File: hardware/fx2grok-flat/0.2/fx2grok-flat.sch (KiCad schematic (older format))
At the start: 32 parts, among them IC1 CY7C68013A-56, J1 Conn_02x05_Odd_Even, P1 pkl_USB_OTG, U1 3.3V, U2 USBLC6-2, U3 DSILC6-4, U4 DSILC6-4, X1 24MHz

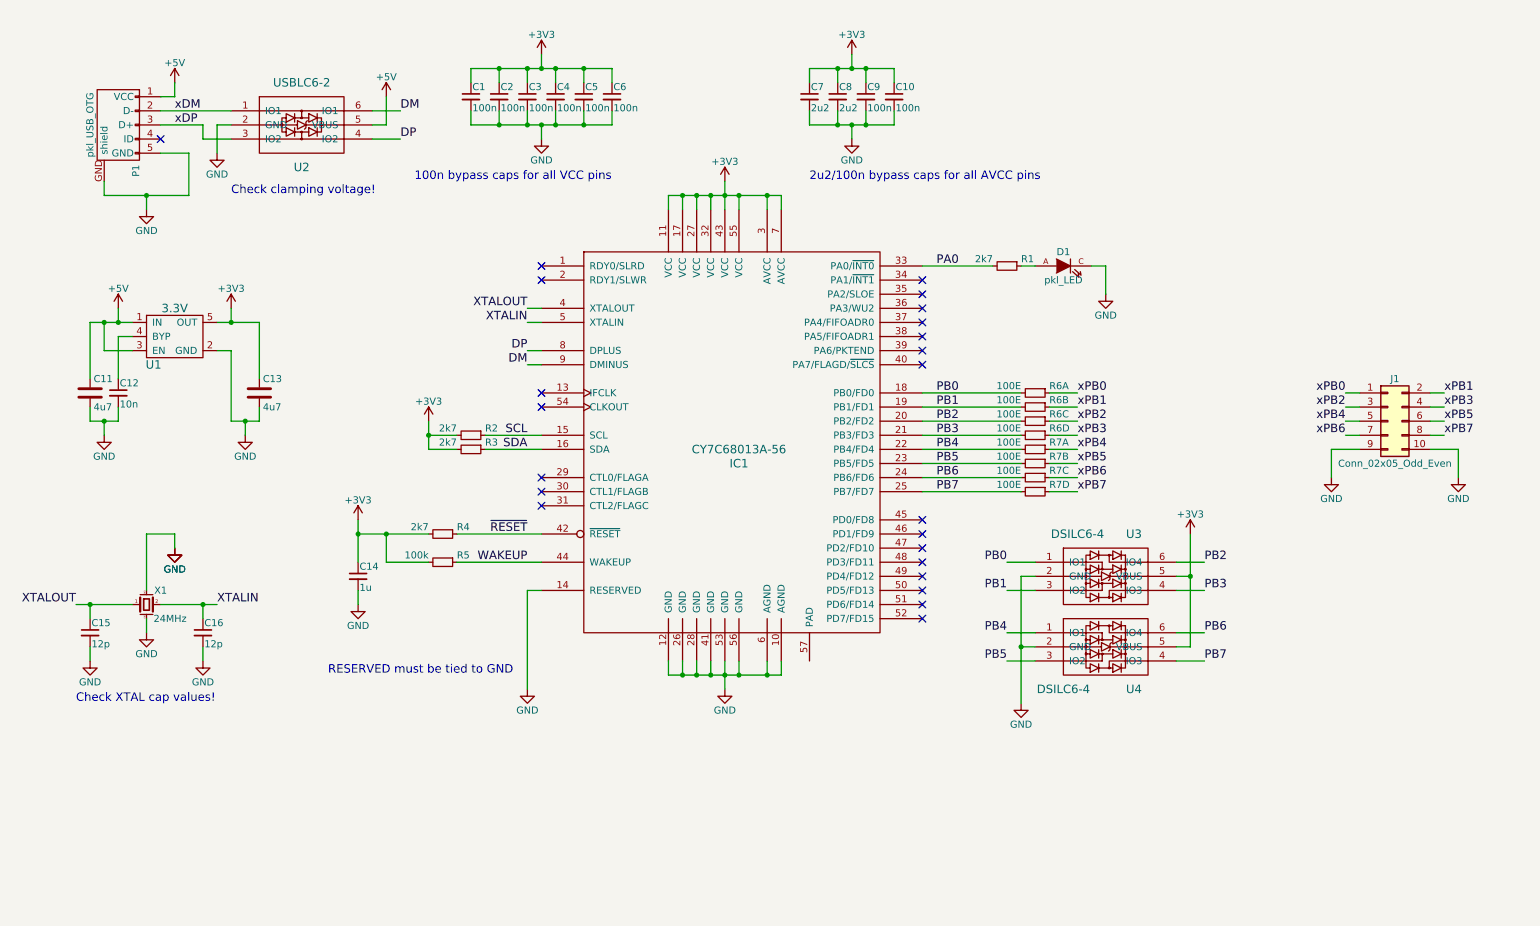
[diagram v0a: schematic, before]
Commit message: Added eeprom and pullups on probe inputs. Started routing.
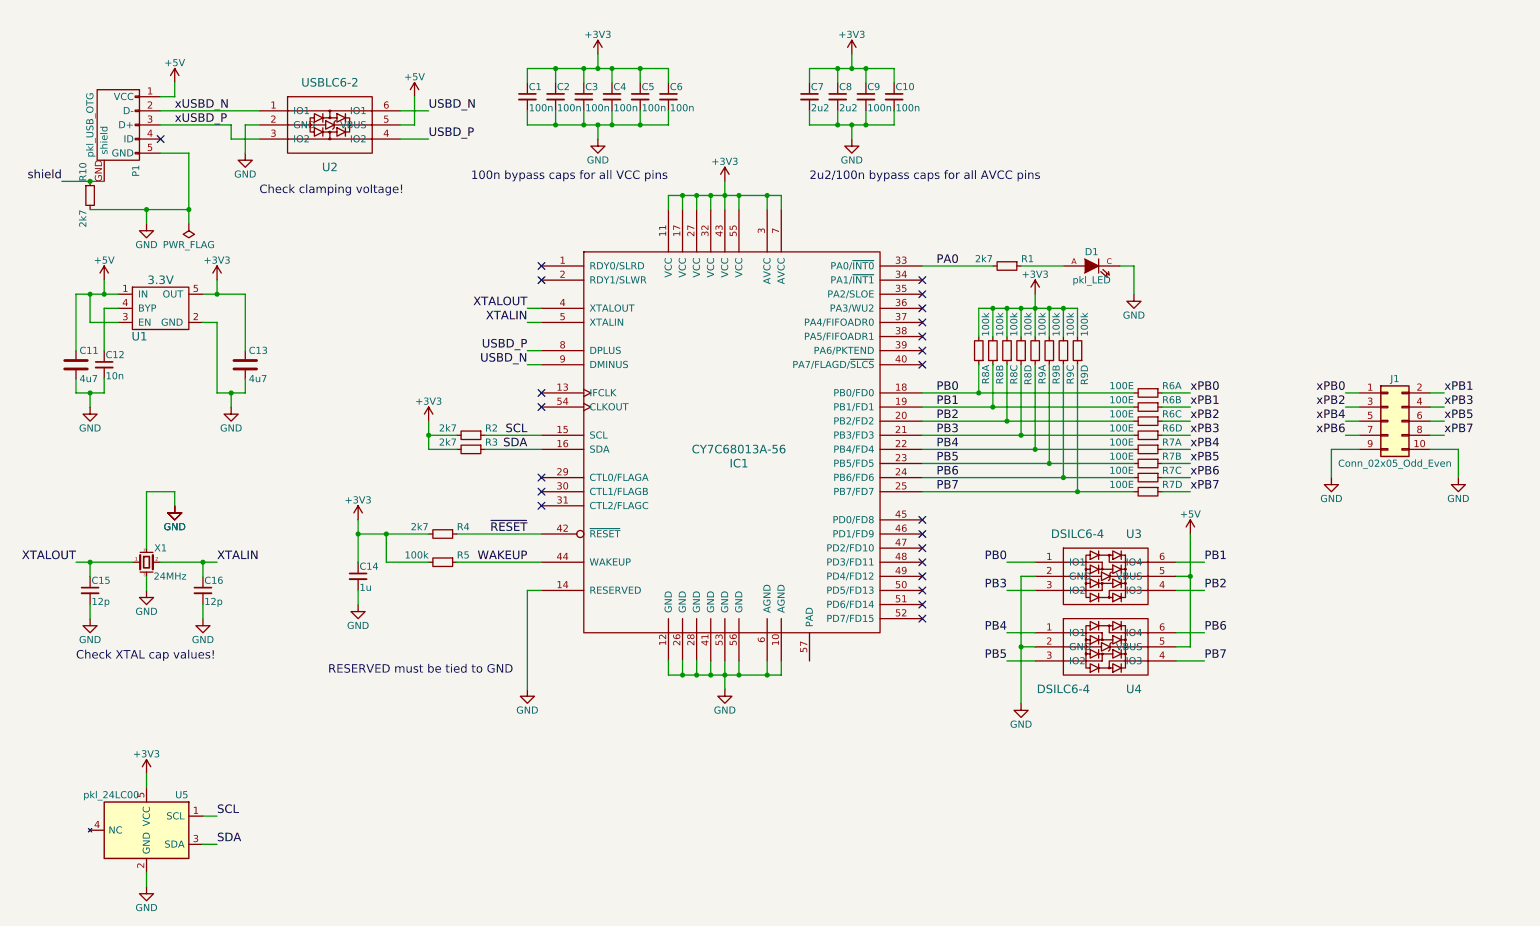
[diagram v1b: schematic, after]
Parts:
- added R10: 2k7, pkl_dipol:R_0402, symbol pkl_R_Small
- added R8, R9: 100k, pkl_dipol:R_Array_Convex_4x0402, symbol pkl_R4_Small
- added U5: pkl_24LC00, pkl_housings_sot:SOT-23-5, symbol pkl_24LC00
- J1: footprint pkl_samtec:FTSH-105-XX-X-D -> pkl_samtec:FTSH-105-XX-X-DV; Source (none) -> ANY
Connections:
- net +3V3: now also R8.2, R8.4, R8.6, R8.8, R9.2, R9.4, R9.6, R9.8, U5.5 (VCC); no longer U3.5 (VBUS), U4.5 (VBUS)
- net +5V: now also U3.5 (VBUS), U4.5 (VBUS)
- net GND: now also R10.2, U5.2 (GND); no longer P1.GND (shield)
- net PB0: now also R8.1
- net PB1: now also U3.6 (IO4), R8.3; no longer U3.3 (IO2)
- net PB2: now also U3.4 (IO3), R8.5; no longer U3.6 (IO4)
- net PB3: now also U3.3 (IO2), R8.7; no longer U3.4 (IO3)
- net PB4: now also R9.1
- net PB5: now also R9.3
- net PB6: now also R9.5
- net PB7: now also R9.7
- net SCL: now also U5.1 (SCL)
- net SDA: now also U5.3 (SDA)
- net DM renamed USBD_N
- net DP renamed USBD_P
- net xDM renamed xUSBD_N
- net xDP renamed xUSBD_P
- new net shield: P1.GND (shield), R10.1
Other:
- moved on the sheet: C1, C11, C12, C13, C15, C16, C2, C3, C4, C5, C6, D1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

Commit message: FX2Grok-flat with new frontend first routing pass.
This is the status of the design as included on esden KiCad LP.
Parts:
- removed R6, R7: 100E, pkl_dipol:R_Array_Convex_4x0402, symbol pkl_R4_Small
- removed U3, U4: DSILC6-4, pkl_housings_sot:SOT-666, symbol DSILC6-4
- added R6: 100k, pkl_dipol:R_0402, symbol pkl_R_Small
- added U3, U4, U6: IP425x-4-TTL, pkl_housings_dfn_qfn:DFN-8-1EP_1.35x1.7mm_Pitch0.4mm, symbol IP425x-4-TTL
- J1: footprint pkl_samtec:FTSH-105-XX-X-DV -> pkl_samtec:TFC-106-02-X-D; symbol Conn_02x05_Odd_Even -> Conn_02x06_Odd_Even
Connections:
- net +3V3: now also R6.1
- net GND: now also IC1.57 (PAD), J1.11 (Pin_11), J1.12 (Pin_12), U3.9, U3.9, U3.9, U3.9, U4.9, U4.9, U4.9, U4.9, U6.9, U6.9; no longer J1.10 (Pin_10), J1.9 (Pin_9)
- net PB0: now also U3.4
- net PB1: now also U3.3
- net PB2: now also U3.2
- net PB3: now also U3.1
- net PB4: now also U4.4
- net PB5: now also U4.3
- net PB6: now also U4.2
- net PB7: now also U4.1
- net xPB0: now also U3.5
- net xPB1: now also U3.6
- net xPB2: now also U3.7
- net xPB3: now also U3.8
- net xPB4: now also U4.5
- net xPB5: now also U4.6
- net xPB6: now also U4.7
- net xPB7: now also U4.8
- net TRIG: now reaches IC1.1 (RDY0/SLRD)
- net TRIG: now also R6.2, U6.1
- net CLK: now reaches IC1.30 (CTL1/FLAGB)
- net CLK: now also U6.3
- net PA1: now reaches IC1.34 (PA1/~INT1)
- net PA1: now also R1.2
- net PA0: no longer names the net of IC1.33 (PA0/~INT0)
- net PA0: no longer R1.2
- new net xCLK: J1.10 (Pin_10), U6.6
- new net xTRIG: J1.9 (Pin_9), U6.8
- no-connect marks 23 -> 21
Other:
- note added: "LED"
- moved on the sheet: C14, D1, IC1, R1, R2, R3, R4, R5, R8A, R8B, R8C, R8D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

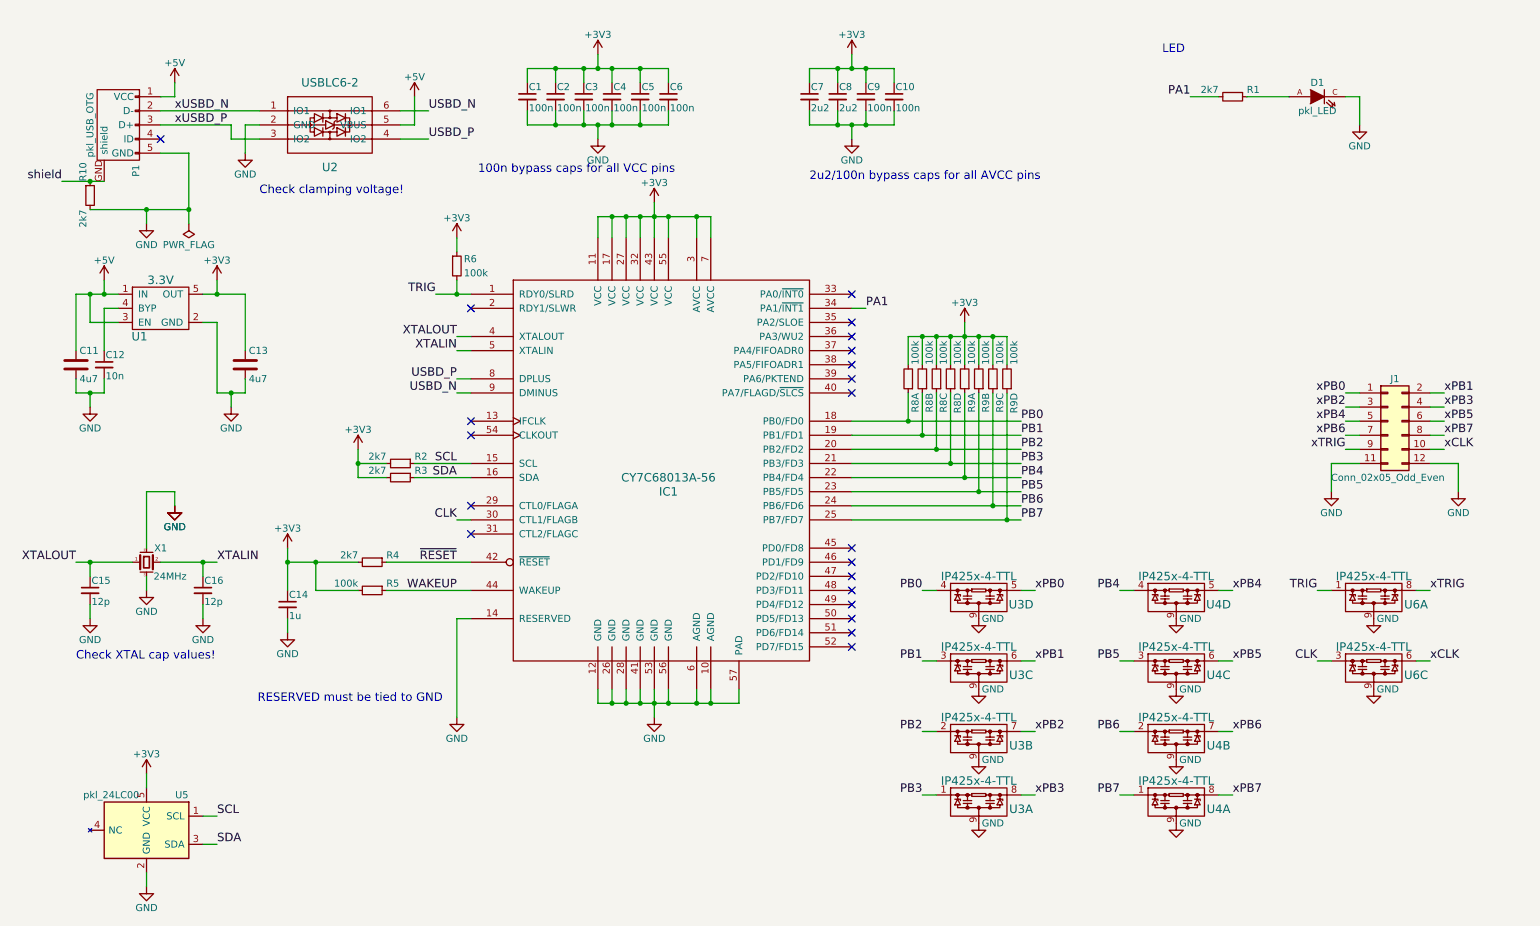
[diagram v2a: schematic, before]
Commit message: Cleaned up and grouped schematic sections.
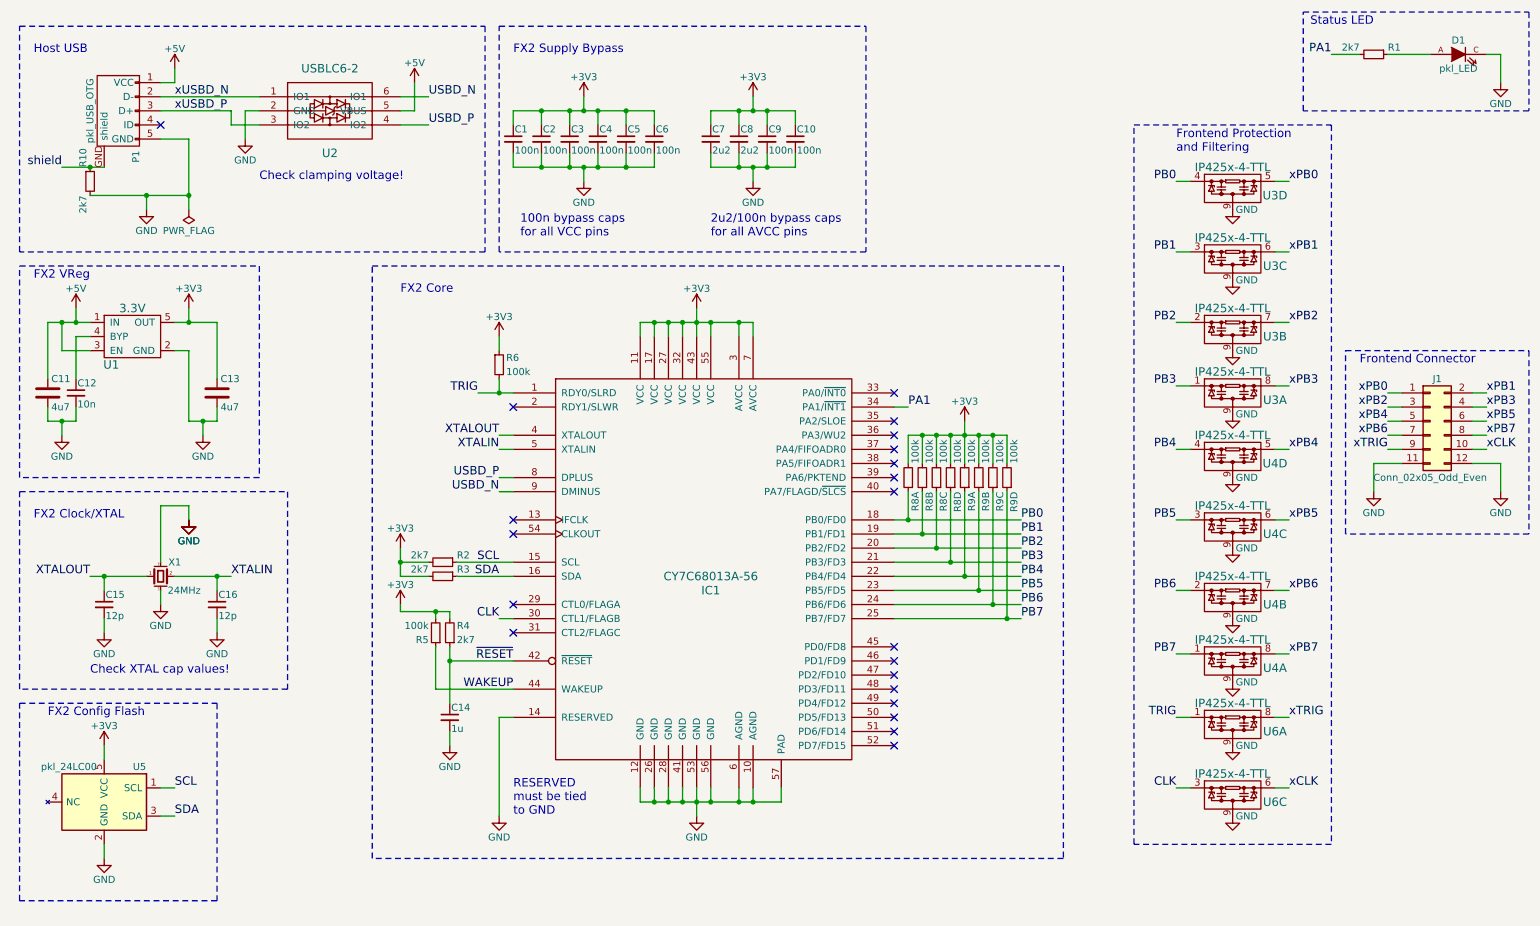
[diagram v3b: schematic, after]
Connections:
- net +3V3: no longer C14.1
- net ~RESET: now also C14.1
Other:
- note added: "100n bypass caps\nfor all VCC pins"
- note added: "2u2/100n bypass caps\nfor all AVCC pins"
- note added: "FX2 Clock/XTAL"
- note added: "FX2 Config Flash"
- note added: "FX2 Core"
- note added: "FX2 Supply Bypass"
- note added: "FX2 VReg"
- note added: "Frontend Connector"
- note added: "Frontend Protection\nand Filtering"
- note added: "Host USB"
- note added: "RESERVED\nmust be tied\nto GND"
- note added: "Status LED"
- note removed: "100n bypass caps for all VCC pins"
- note removed: "2u2/100n bypass caps for all AVCC pins"
- note removed: "LED"
- note removed: "RESERVED must be tied to GND"
- moved on the sheet: C1, C10, C11, C12, C13, C14, C15, C16, C2, C3, C4, C5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

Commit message: More cleanup of the board routing.
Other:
- note removed: "Check clamping voltage!"
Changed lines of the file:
@@
 	1    0    0    -1
 $EndComp
-Text Notes 2200 1700 0    60   ~ 0
-Check clamping voltage!
 Text Label 7600 4600 0    60   ~ 0
 PB5

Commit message: Added BOM unique part keys and made a few minor adjustments.
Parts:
- C1, C10, C2, C3, C4, C5, C6, C9: Key (none) -> cap-cer-0402-100n
- C11, C13: Key (none) -> cap-cer-0603-4u7
- C12: Key (none) -> cap-cer-0402-10n
- C14: Key (none) -> cap-cer-0401-1u
- C15, C16: value 12p -> 10p; Key (none) -> cap-cer-0402-10p
- C7, C8: Key (none) -> cap-cer-0402-2u2
- D1: value pkl_LED -> GRN; Key (none) -> led-0603-grn
- IC1: Key (none) -> ic-cy7c68013a-56; Source (none) -> ANY
- J1: Key (none) -> conn-smd-TFC-0.05in-6-2; MFN (none) -> TFC-106-02-X-D; Manufacturer (none) -> Samtec
- P1: Key (none) -> conn-smd-usb-micro-b; Source (none) -> ANY
- R1, R2, R3, R4: Key (none) -> res-0402-2k7
- R10: value 2k7 -> 1m; Key (none) -> res-0402-1m
- R5, R6: Key (none) -> res-0402-100k
- R8, R9: Key (none) -> res-0402cv-array-4-100k
- U1: Key (none) -> vreg-sot23-5-3v3
- U2: Key (none) -> tvs-diode-sot666
- U3, U4: Description (none) -> Quad ESD EMI filter 800MHz; Key (none) -> filter-dfn8-IP425x; Source (none) -> ANY
- U5: value pkl_24LC00 -> 24LC00; Characteristics (none) -> 128 byte; Description (none) -> 24LC00 128byte eeprom; Key (none) -> ic-sot-23-5-128-eeprom
- U6: Description (none) -> Quad ESD EMI filter 800MHz; Key (none) -> filter-dfn8-IP425x
- X1: Key (none) -> xtal-abm8-24mhz
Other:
- note added: "128 Byte Config EEPROM"
